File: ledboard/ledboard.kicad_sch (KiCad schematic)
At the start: 41 parts, among them J1 Jack-DC, U1 TPS54332DDA, U2 TPS2121, U8 TPS7A5301BRPSR

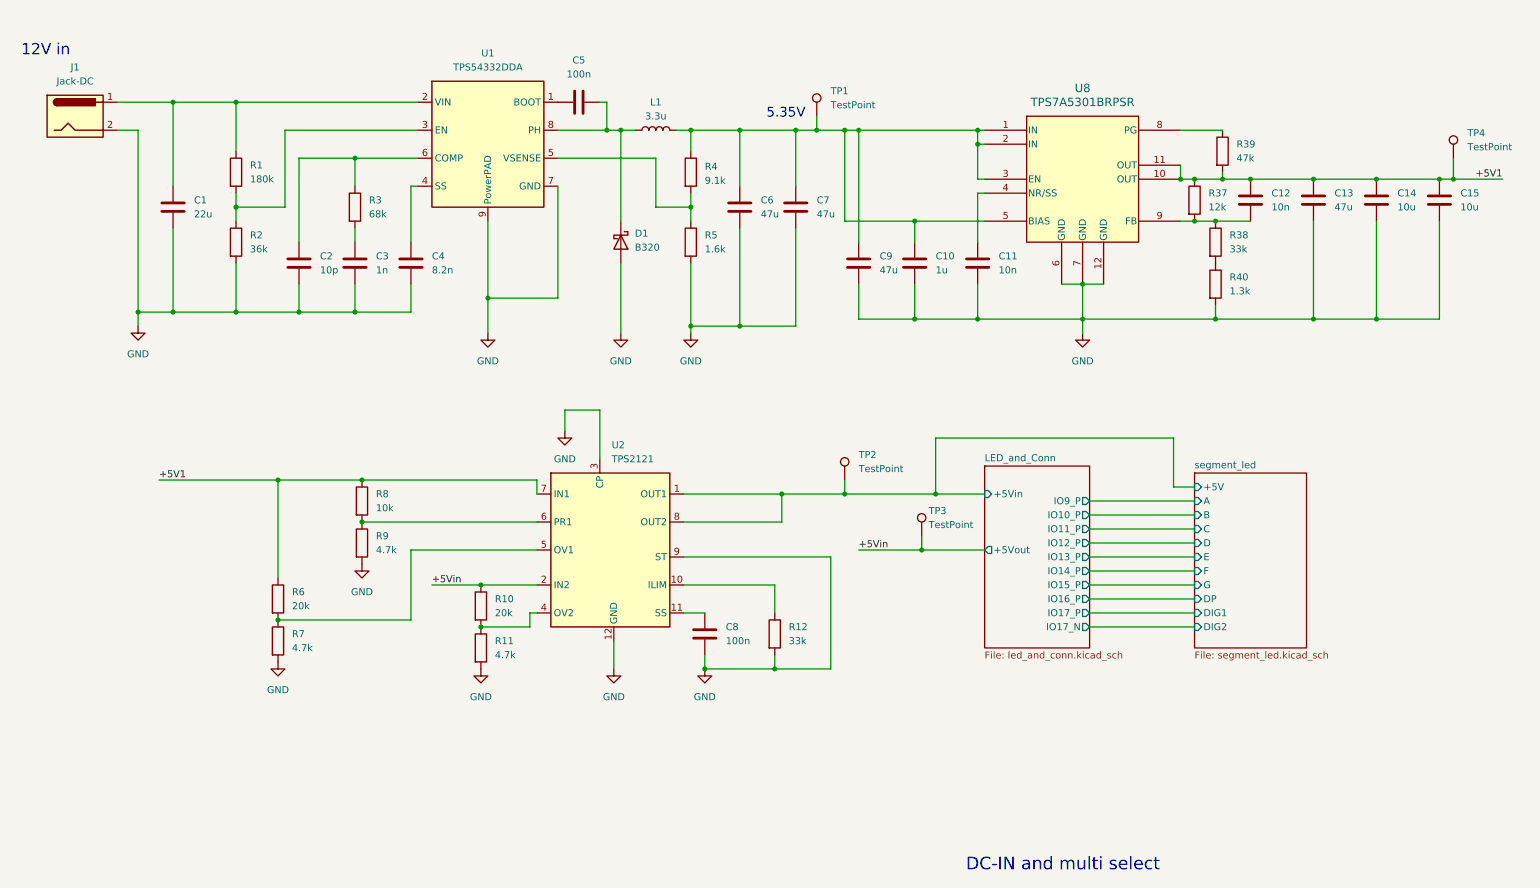
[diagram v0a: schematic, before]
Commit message: 各種定数見直し,TPS2121の前後にデカップリングコンデンサを配置.
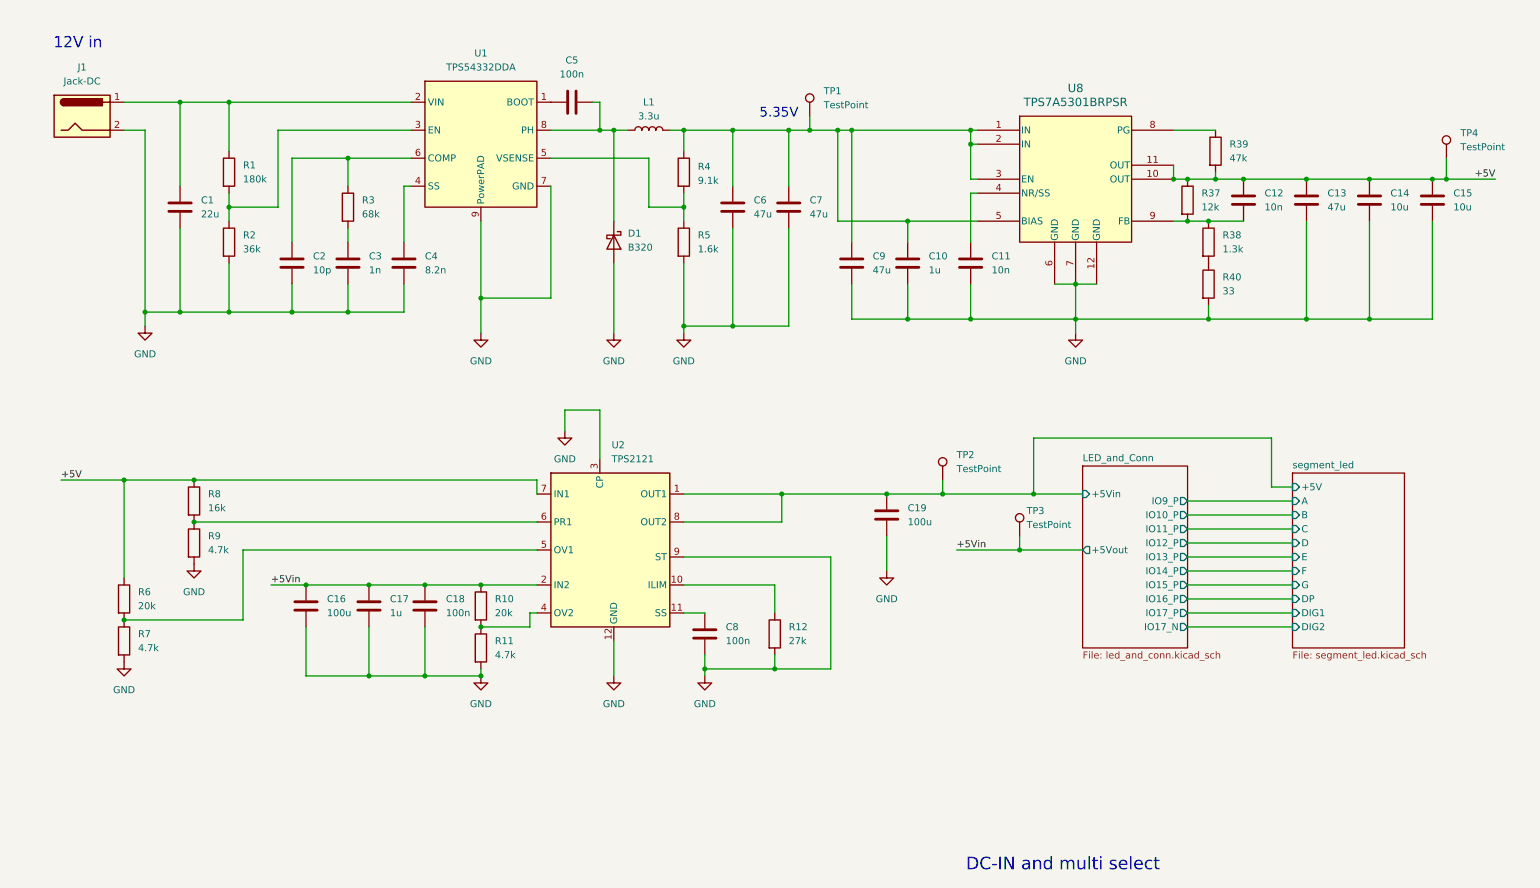
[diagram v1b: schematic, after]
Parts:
- added C16, C19: 100u, symbol Device:C
- added C17: 1u, symbol Device:C
- added C18: 100n, symbol Device:C
- R12: value 33k -> 27k
- R38: value 33k -> 1.3k
- R40: value 1.3k -> 33
- R8: value 10k -> 16k
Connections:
- net +5Vin: now also C16.1, C17.1, C18.1
- net GND: now also C16.2, C17.2, C18.2, C19.2
- net LED_and_Conn/+5Vin: now also C19.1
- net +5V1 renamed +5V
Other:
- moved on the sheet: C1, C10, C11, C12, C13, C14, C15, C2, C3, C4, C5, C6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

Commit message: 部品の再アノテーションを行う.
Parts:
- renumbered C11 to C10, C12 to C11, C13 to C12, C14 to C13, C15 to C14, C16 to C15, C17 to C16, C18 to C17, C8 to C18, C19 to C18, C9 to C8, C10 to C9, R8 to R10, R9 to R11, R6 to R12, R7 to R13, R10 to R14, R11 to R15, R12 to R16, R39 to R6, R37 to R7, R38 to R8, R40 to R9, TP4 to TP2, TP2 to TP3, TP3 to TP4, U8 to U2, U2 to U3

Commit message: 部品が決まったので,コミットします.
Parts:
- removed J1: Jack-DC, symbol Connector:Jack-DC
- added J1: Barrel_Jack_Switch, MyLib:MPD_EJ503A, symbol Connector:Barrel_Jack_Switch
- added J3: Conn_01x02, Connector_PinHeader_2.54mm:PinHeader_1x02_P2.54mm_Vertical, symbol Connector_Generic:Conn_01x02
- C10: footprint Capacitor_SMD:C_1206_3216Metric -> Capacitor_SMD:C_01005_0402Metric; MPN GRM31CR61C476ME44 -> GRM022R61C103ME01
- C11: footprint (none) -> Capacitor_SMD:C_01005_0402Metric; MPN (none) -> GRM022R61C103ME01; Manufacturer (none) -> Murata
- C12: footprint (none) -> Capacitor_SMD:C_1206_3216Metric; MPN (none) -> GRM31CR61C476ME44; Manufacturer (none) -> Murata
- C13, C14: footprint (none) -> Capacitor_SMD:C_0603_1608Metric; MPN (none) -> GRM188R61C106MA73; Manufacturer (none) -> Murata
- C15: footprint (none) -> Capacitor_SMD:C_1210_3225Metric; MPN (none) -> GRM32ER61A107ME20; Manufacturer (none) -> Murata
- C16: footprint (none) -> Capacitor_SMD:C_0402_1005Metric; MPN (none) -> GRM155C71A105KE11; Manufacturer (none) -> Murata
- C17, C18: footprint (none) -> Capacitor_SMD:C_0201_0603Metric; MPN (none) -> GRM033C81A104ME14; Manufacturer (none) -> Murata
- C19: renamed from C18; footprint (none) -> Capacitor_SMD:C_1210_3225Metric; MPN (none) -> GRM32ER61A107ME20; Manufacturer (none) -> Murata
- C2: MPN GRM1555C2A100JA01 -> GRM0222C1C100JA03
- C3: footprint (none) -> Capacitor_SMD:C_0201_0603Metric; MPN (none) -> GRM033R71C102KA01; Manufacturer (none) -> Murata
- C4: footprint (none) -> Capacitor_SMD:C_0201_0603Metric; MPN (none) -> GRM033B11A822JA01; Manufacturer (none) -> Murata
- C5: footprint (none) -> Capacitor_SMD:C_0201_0603Metric; MPN (none) -> GRM033C81E104ME14; Manufacturer (none) -> Murata
- C9: footprint Capacitor_SMD:C_1206_3216Metric -> Capacitor_SMD:C_0402_1005Metric; MPN GRM31CR61C476ME44 -> GRM155B31C105KA12
- L1: footprint (none) -> MyLib:SPM7054VC-3R3M-D
- R1: MPN (none) -> RC0603FR-07180KL; Manufacturer (none) -> YAGEO
- R10: footprint (none) -> Resistor_SMD:R_0603_1608Metric; MPN (none) -> RC0603FR-0716KL; Manufacturer (none) -> YAGEO
- R11, R13, R15: footprint (none) -> Resistor_SMD:R_0603_1608Metric; MPN (none) -> RC0603FR-074K7L; Manufacturer (none) -> YAGEO
- R12, R14: footprint (none) -> Resistor_SMD:R_0603_1608Metric; MPN (none) -> RC0603FR-0720KL; Manufacturer (none) -> YAGEO
- R16: footprint (none) -> Resistor_SMD:R_0603_1608Metric; MPN (none) -> RC0603FR-0727KL; Manufacturer (none) -> YAGEO
- R2: MPN (none) -> RC0603FR-0736KL; Manufacturer (none) -> YAGEO
- R3: footprint (none) -> Resistor_SMD:R_0603_1608Metric; MPN (none) -> RC0603FR-0768KL; Manufacturer (none) -> YAGEO
- R4: footprint (none) -> Resistor_SMD:R_0603_1608Metric; MPN (none) -> RC0603FR-0769K1L; Manufacturer (none) -> YAGEO
- R5: footprint (none) -> Resistor_SMD:R_0603_1608Metric; MPN (none) -> RC0603FR-071K6L; Manufacturer (none) -> YAGEO
- R6: footprint (none) -> Resistor_SMD:R_0603_1608Metric; MPN (none) -> RC0603FR-0747KL; Manufacturer (none) -> YAGEO
- R7: footprint (none) -> Resistor_SMD:R_0603_1608Metric; MPN (none) -> RC0603FR-0712KL; Manufacturer (none) -> YAGEO
- R8: footprint (none) -> Resistor_SMD:R_0603_1608Metric; MPN (none) -> RC0603FR-071K3L; Manufacturer (none) -> YAGEO
- R9: footprint (none) -> Resistor_SMD:R_0603_1608Metric; MPN (none) -> RC0603FR-0733RL; Manufacturer (none) -> YAGEO
- TP1, TP2, TP3, TP4: footprint (none) -> TestPoint:TestPoint_Keystone_5000-5004_Miniature; MPN (none) -> 5002; Manufacturer (none) -> keystone
- U2: MPN (none) -> TPS7A5301BRPSR; Manufacturer (none) -> TI
- U3: MPN TPS2121 -> TPS2121RUXR
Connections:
- net +5Vin is gone; now on net +5V: C15.1, C16.1, C17.1, R14.1, TP4.1, U3.2 (IN2)
- net +5V: no longer C11.1, C12.1, C13.1, C14.1, R10.1, R12.1, R6.2, R7.1, TP2.1, U2.10 (OUT), U2.11 (OUT), U3.7 (IN1)
- net GND: now also J1.2, J3.2 (Pin_2)
- net at C1.1, R1.1, U1.2 (VIN): now also J1.1
- net LED_and_Conn/+5Vin renamed LED_and_Conn/+5V_VCC
- new net +5V_LOCAL: C11.1, C12.1, C13.1, C14.1, J3.1 (Pin_1), R10.1, R12.1, R6.2, R7.1, TP2.1, U2.10 (OUT), U2.11 (OUT), U3.7 (IN1)
- no-connect marks 0 -> 1
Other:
- sheet LED_and_Conn ports: added +5V, +5V_VCC; removed +5Vin, +5Vout
- sheet segment_led ports: added +5V_VCC; removed +5V
- note added: "5.001V"
- moved on the sheet: C10, C11, C12, C13, C14, C15, C16, C17, C18, C19, R10, R11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

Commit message: ERC解消まで.
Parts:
- U3: MPN TPS2121RUXR -> TPS2121
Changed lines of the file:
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@@
 			)
 		)
-		(property "Datasheet" "https://pim.murata.com/asset/pim4/ceramicCapacitorSMD/GRM022R61E103ME01-01A-JP_PDF_CERAMICCAPACITORSMD?lastModifiedDatetime=20250813135319"
+		(property "Datasheet" "~"
 			(at 233.68 52.07 0)
 			(effects
@@
 			)
 		)
-		(property "Datasheet" "https://www.memoryprotectiondevices.com/datasheets/EJ503A/EJ503A-datasheet.pdf"
+		(property "Datasheet" "~"
 			(at 25.4 37.846 0)
 			(effects
@@
 			)
 		)
-		(property "Datasheet" "https://yageogroup.com/content/datasheet/asset/file/PYU-RC_GROUP_51_ROHS_L"
+		(property "Datasheet" "~"
 			(at 39.37 143.51 0)
 			(effects
@@
 			)
 		)
-		(property "Datasheet" "https://pim.murata.com/asset/pim4/ceramicCapacitorSMD/GRM033B11A222JA01-01A-JP_PDF_CERAMICCAPACITORSMD?lastModifiedDatetime=20250813141149"
+		(property "Datasheet" "~"
 			(at 82.55 63.5 0)
 			(effects
@@
 			)
 		)
-		(property "Datasheet" "https://pim.murata.com/asset/pim4/ceramicCapacitorSMD/GRM155B31C105KA12-01A-JP_PDF_CERAMICCAPACITORSMD?lastModifiedDatetime=20250813144309"
+		(property "Datasheet" "~"
 			(at 173.99 63.5 0)
 			(effects
@@
 			)
 		)
-		(property "Datasheet" "https://pim.murata.com/asset/pim4/ceramicCapacitorSMD/GRM033R71C102KA01-01A-JP_PDF_CERAMICCAPACITORSMD?lastModifiedDatetime=20250813141657"
+		(property "Datasheet" "~"
 			(at 72.39 63.5 0)
 			(effects
@@
 			)
 		)
-		(property "Datasheet" "https://www.keyelco.com/userAssets/file/K75p62.pdf"
+		(property "Datasheet" "~"
 			(at 275.59 44.45 0)
 			(effects
@@
 			)
 		)
-		(property "Datasheet" "https://pim.murata.com/asset/pim4/ceramicCapacitorSMD/GRM033C81A104ME14-01A-JP_PDF_CERAMICCAPACITORSMD?lastModifiedDatetime=20250813141354"
+		(property "Datasheet" "~"
 			(at 142.24 142.24 0)
 			(effects
@@
 			)
 		)
-		(property "Datasheet" "https://yageogroup.com/content/datasheet/asset/file/PYU-RC_GROUP_51_ROHS_L"
+		(property "Datasheet" "~"
 			(at 228.6 43.18 0)
 			(effects
@@
 			)
 		)
-		(property "Datasheet" "https://pim.murata.com/asset/pim4/ceramicCapacitorSMD/GRM32ER61A107ME20-01A-JP_PDF_CERAMICCAPACITORSMD?lastModifiedDatetime=20250813153035"
+		(property "Datasheet" "~"
 			(at 69.85 137.16 0)
 			(effects
@@
 			)
 		)
-		(property "Datasheet" "https://pim.murata.com/asset/pim4/ceramicCapacitorSMD/GRM188R61C106MA73-01A-JP_PDF_CERAMICCAPACITORSMD?lastModifiedDatetime=20250813150719"
+		(property "Datasheet" "~"
 			(at 256.54 52.07 0)
 			(effects
@@
 			)
 		)
-		(property "Datasheet" "https://pim.murata.com/asset/pim4/ceramicCapacitorSMD/GRM022R61E103ME01-01A-JP_PDF_CERAMICCAPACITORSMD?lastModifiedDatetime=20250813135319"
+		(property "Datasheet" "~"
 			(at 184.15 63.5 0)
 			(effects
@@
 			)
 		)
-		(property "Datasheet" "https://www.keyelco.com/userAssets/file/K75p62.pdf"
+		(property "Datasheet" "~"
 			(at 204.47 124.46 0)
 			(effects
@@
 			)
 		)
-		(property "Datasheet" "https://pim.murata.com/asset/pim4/ceramicCapacitorSMD/GRM31CC71E226ME15-01A-JP_PDF_CERAMICCAPACITORSMD?lastModifiedDatetime=20250813152619"
+		(property "Datasheet" "~"
 			(at 41.91 53.34 0)
 			(effects
@@
 			)
 		)
-		(property "Datasheet" "https://yageogroup.com/content/datasheet/asset/file/PYU-RC_GROUP_51_ROHS_L"
+		(property "Datasheet" "~"
 			(at 39.37 135.89 0)
 			(effects
@@
 			)
 		)
-		(property "Datasheet" "https://yageogroup.com/content/datasheet/asset/file/PYU-RC_GROUP_51_ROHS_L"
+		(property "Datasheet" "~"
 			(at 227.33 59.69 0)
 			(effects
@@
 			)
 		)
-		(property "Datasheet" "https://www.keyelco.com/userAssets/file/K75p62.pdf"
+		(property "Datasheet" "~"
 			(at 190.5 114.3 0)
 			(effects
@@
 			)
 		)
-		(property "Datasheet" "https://pim.murata.com/asset/pim4/ceramicCapacitorSMD/GRM188R61C106MA73-01A-JP_PDF_CERAMICCAPACITORSMD?lastModifiedDatetime=20250813150719"
+		(property "Datasheet" "~"
 			(at 267.97 52.07 0)
 			(effects
@@
 			)
 		)
-		(property "Datasheet" "https://pim.murata.com/asset/pim4/ceramicCapacitorSMD/GRM32ER61A107ME20-01A-JP_PDF_CERAMICCAPACITORSMD?lastModifiedDatetime=20250813153035"
+		(property "Datasheet" "~"
 			(at 175.26 120.65 0)
 			(effects
@@
 			)
 		)
-		(property "Datasheet" "https://pim.murata.com/asset/pim4/ceramicCapacitorSMD/GRM31CR61C476ME44-01A-JP_PDF_CERAMICCAPACITORSMD?lastModifiedDatetime=20250813152638"
+		(property "Datasheet" "~"
 			(at 142.24 53.34 0)
 			(effects
@@
 			)
 		)
-		(property "Datasheet" "https://pim.murata.com/asset/pim4/ceramicCapacitorSMD/GRM31CR61C476ME44-01A-JP_PDF_CERAMICCAPACITORSMD?lastModifiedDatetime=20250813152638"
+		(property "Datasheet" "~"
 			(at 152.4 53.34 0)
 			(effects
@@
 			)
 		)
-		(property "Datasheet" "https://pim.murata.com/asset/pim4/ceramicCapacitorSMD/GRM31CR61C476ME44-01A-JP_PDF_CERAMICCAPACITORSMD?lastModifiedDatetime=20250813152638"
+		(property "Datasheet" "~"
 			(at 245.11 52.07 0)
 			(effects
@@
 			)
 		)
-		(property "Datasheet" "https://www.keyelco.com/userAssets/file/K75p62.pdf"
+		(property "Datasheet" "~"
 			(at 161.29 36.83 0)
 			(effects
@@
 			)
 		)
-		(property "Datasheet" "https://yageogroup.com/content/datasheet/asset/file/PYU-RC_GROUP_51_ROHS_L"
+		(property "Datasheet" "~"
 			(at 50.8 59.69 0)
 			(effects
@@
 			)
 		)
-		(property "Datasheet" "https://www.ti.com/jp/lit/ds/symlink/tps54332.pdf?ts=1774599358950&ref_url=https%253A%252F%252Fwww.ti.com%252Fproduct%252Fja-jp%252FTPS54332%253Futm_source%253Dgoogle%2526utm_medium%253Dcpc%2526utm_campaign%253Dapp-null-null-gpn_jp-cpc-pf-google-jp_jp_cons%2526utm_content%253DTPS54332%2526ds_k%253DTPS54332%2526DCM%253Dyes%2526gclsrc%253Daw.ds%2526gad_source%253D1%2526gad_campaignid%253D20279248515%2526gclid%253DCj0KCQjw1ZjOBhCmARIsADDuFTBmD5gUQSDSVcVDqtlcqWftM3LiZUXBOSejrsmSzrKRocTvUMsoHYIaAuFjEALw_wcB"
+		(property "Datasheet" "https://www.ti.com/product/ja-jp/TPS54332#cad-cae-symbols"
 			(at 96.52 41.91 0)
 			(effects
@@
 			)
 		)
-		(property "Description" ""
+		(property "Description" "DC-DC Converter"
 			(at 96.52 41.91 0)
 			(effects
@@
 			)
 		)
-		(property "Datasheet" "https://pim.murata.com/asset/pim4/ceramicCapacitorSMD/GRM155C71A105KE11-01A-JP_PDF_CERAMICCAPACITORSMD?lastModifiedDatetime=20260115145428"
+		(property "Datasheet" "~"
 			(at 81.28 137.16 0)
 			(effects
@@
 			)
 		)
-		(property "Datasheet" "https://yageogroup.com/content/datasheet/asset/file/PYU-RC_GROUP_51_ROHS_L"
+		(property "Datasheet" "~"
 			(at 154.94 142.24 0)
 			(effects
@@
 			)
 		)
-		(property "Datasheet" "https://pim.murata.com/asset/pim4/ceramicCapacitorSMD/GRM033C81A104ME14-01A-JP_PDF_CERAMICCAPACITORSMD?lastModifiedDatetime=20250813141354"
+		(property "Datasheet" "~"
 			(at 91.44 137.16 0)
 			(effects
@@
 			)
 		)
-		(property "Datasheet" "https://pim.murata.com/asset/pim4/ceramicCapacitorSMD/GRM033C81E104ME14-01A-JP_PDF_CERAMICCAPACITORSMD?lastModifiedDatetime=20250813141359"
+		(property "Datasheet" "~"
 			(at 113.03 34.29 0)
 			(effects
@@
 			)
 		)
-		(property "Datasheet" "https://yageogroup.com/content/datasheet/asset/file/PYU-RC_GROUP_51_ROHS_L"
+		(property "Datasheet" "~"
 			(at 101.6 137.16 0)
 			(effects
@@
 			)
 		)
-		(property "Datasheet" "https://yageogroup.com/content/datasheet/asset/file/PYU-RC_GROUP_51_ROHS_L"
+		(property "Datasheet" "~"
 			(at 50.8 46.99 0)
 			(effects
@@
 			)
 		)
-		(property "Datasheet" "https://yageogroup.com/content/datasheet/asset/file/PYU-RC_GROUP_51_ROHS_L"
+		(property "Datasheet" "~"
 			(at 227.33 67.31 0)
 			(effects
@@
 			)
 		)
-		(property "Datasheet" "https://yageogroup.com/content/datasheet/asset/file/PYU-RC_GROUP_51_ROHS_L"
+		(property "Datasheet" "~"
 			(at 224.79 52.07 0)
 			(effects
@@
 			)
 		)
-		(property "Datasheet" "https://yageogroup.com/content/datasheet/asset/file/PYU-RC_GROUP_51_ROHS_L"
+		(property "Datasheet" "~"
 			(at 101.6 144.78 0)
 			(effects
@@
 			)
 		)
-		(property "Datasheet" "https://yageogroup.com/content/datasheet/asset/file/PYU-RC_GROUP_51_ROHS_L"
+		(property "Datasheet" "~"
 			(at 133.35 59.69 0)
 			(effects
@@
 			)
 		)
-		(property "Datasheet" "https://pim.murata.com/asset/pim4/ceramicCapacitorSMD/GRM0222C1C100JA03-01A-JP_PDF_CERAMICCAPACITORSMD?lastModifiedDatetime=20250813133405"
+		(property "Datasheet" "~"
 			(at 62.23 63.5 0)
 			(effects
@@
 			)
 		)
-		(property "Datasheet" "https://yageogroup.com/content/datasheet/asset/file/PYU-RC_GROUP_51_ROHS_L"
+		(property "Datasheet" "~"
 			(at 49.53 118.11 0)
 			(effects
@@
 			)
 		)
-		(property "MPN" "TPS2121RUXR"
+		(property "MPN" "TPS2121"
 			(at 124.46 123.19 0)
 			(effects
@@
 			)
 		)
-		(property "Datasheet" "https://yageogroup.com/content/datasheet/asset/file/PYU-RC_GROUP_51_ROHS_L"
+		(property "Datasheet" "~"
 			(at 133.35 46.99 0)
 			(effects
@@
 			)
 		)
-		(property "Datasheet" "https://product.tdk.com/system/files/dam/doc/product/inductor/inductor/smd/catalog/inductor_automotive_power_spm7054vc-d_en.pdf"
+		(property "Datasheet" "~"
 			(at 127 39.37 0)
 			(effects
@@
 			)
 		)
-		(property "Datasheet" "https://pim.murata.com/asset/pim4/ceramicCapacitorSMD/GRM31CR61C476ME44-01A-JP_PDF_CERAMICCAPACITORSMD?lastModifiedDatetime=20250813152638"
+		(property "Datasheet" "~"
 			(at 163.83 63.5 0)
 			(effects
@@
 			)
 		)
-		(property "Datasheet" "https://www.diodes.com/datasheet/download/B320.pdf"
+		(property "Datasheet" "http://www.jameco.com/Jameco/Products/ProdDS/1538777.pdf"
 			(at 120.65 59.69 0)
 			(effects
@@
 			)
 		)
-		(property "Datasheet" "https://yageogroup.com/content/datasheet/asset/file/PYU-RC_GROUP_51_ROHS_L"
+		(property "Datasheet" "~"
 			(at 72.39 53.34 0)
 			(effects
@@
 			)
 		)
-		(property "Datasheet" "https://yageogroup.com/content/datasheet/asset/file/PYU-RC_GROUP_51_ROHS_L"
+		(property "Datasheet" "~"
 			(at 49.53 125.73 0)
 			(effects

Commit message: 部品変更とアートワークの修正.
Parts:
- C10: footprint Capacitor_SMD:C_01005_0402Metric -> Capacitor_SMD:C_0402_1005Metric; MPN GRM022R61C103ME01 -> GRM155R71C103KA01D
- C2: footprint Capacitor_SMD:C_01005_0402Metric -> Capacitor_SMD:C_0402_1005Metric; MPN GRM0222C1C100JA03 -> GRM1555C1E100JA01D
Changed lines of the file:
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@@
 			)
 		)
-		(property "Footprint" "Capacitor_SMD:C_01005_0402Metric"
+		(property "Footprint" "Capacitor_SMD:C_0402_1005Metric"
 			(at 185.1152 67.31 0)
 			(effects
@@
 			)
 		)
-		(property "MPN" "GRM022R61C103ME01"
+		(property "MPN" "GRM155R71C103KA01D"
 			(at 184.15 63.5 0)
 			(effects
@@
 			)
 		)
-		(property "Footprint" "Capacitor_SMD:C_01005_0402Metric"
+		(property "Footprint" "Capacitor_SMD:C_0402_1005Metric"
 			(at 63.1952 67.31 0)
 			(effects
@@
 			)
 		)
-		(property "MPN" "GRM0222C1C100JA03"
+		(property "MPN" "GRM1555C1E100JA01D"
 			(at 62.23 63.5 0)
 			(effects
